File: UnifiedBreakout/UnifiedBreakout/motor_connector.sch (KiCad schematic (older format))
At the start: 1 part, among them J15 RJ45

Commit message: Unified breakout schematic "done"
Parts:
- J7: renamed from J15; footprint (none) -> Connector_RJ:RJ45_Ninigi_GE
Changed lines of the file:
@@
 $Descr A4 11693 8268
 encoding utf-8
-Sheet 2 5
+Sheet 3 20
 Title ""
 Date ""
@@
 $EndDescr
 $Comp
-L Connector:RJ45 J15
+L Connector:RJ45 J7
 U 1 1 5E675BA7
 P 5400 3350
-AR Path="/5E6754F3/5E675BA7" Ref="J15"  Part="1"
+AR Path="/5E6754F3/5E675BA7" Ref="J7"  Part="1"
 AR Path="/5E67ECBC/5E675BA7" Ref="J?"  Part="1"
-AR Path="/5E67FD54/5E675BA7" Ref="J?"  Part="1"
-AR Path="/5E67FFE4/5E675BA7" Ref="J?"  Part="1"
-F 0 "J?" H 5070 3354 50  0000 R CNN
+AR Path="/5E67FD54/5E675BA7" Ref="J8"  Part="1"
+AR Path="/5E67FFE4/5E675BA7" Ref="J9"  Part="1"
+F 0 "J9" H 5070 3354 50  0000 R CNN
 F 1 "RJ45" H 5070 3445 50  0000 R CNN
-F 2 "" V 5400 3375 50  0001 C CNN
+F 2 "Connector_RJ:RJ45_Ninigi_GE" V 5400 3375 50  0001 C CNN
 F 3 "~" V 5400 3375 50  0001 C CNN
 	1    5400 3350
@@
 Text HLabel 3500 3450 0    50   Input ~ 0
 ENABLE
-Text HLabel 3500 3650 0    50   Output ~ 0
+Text HLabel 3500 3650 0    50   Input ~ 0
 ALARM
 Text HLabel 4800 4000 3    50   UnSpc ~ 0

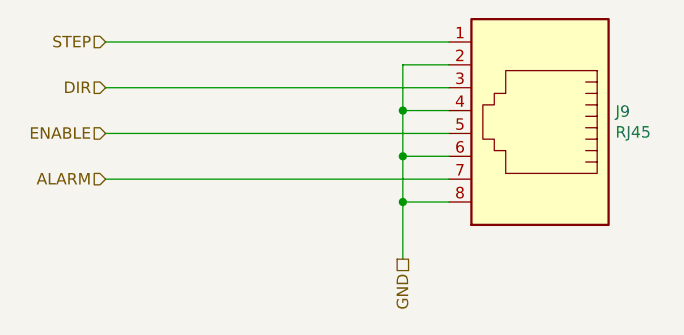
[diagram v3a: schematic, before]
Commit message: More placement, add some custom parts
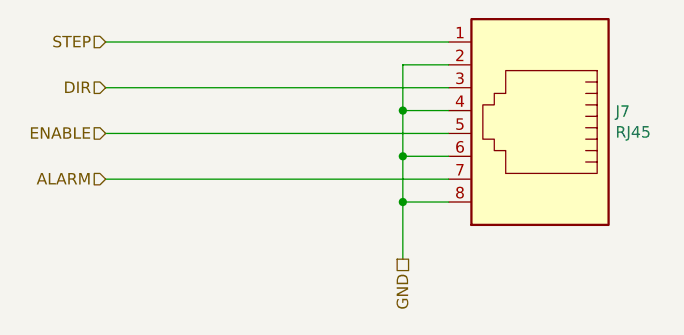
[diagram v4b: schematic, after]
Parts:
- J7: footprint Connector_RJ:RJ45_Ninigi_GE -> Stewart:SS6488SANF1
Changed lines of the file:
@@
 $Descr A4 11693 8268
 encoding utf-8
-Sheet 4 18
+Sheet 2 18
 Title ""
 Date ""
@@
 AR Path="/5E67FD54/5E675BA7" Ref="J8"  Part="1"
 AR Path="/5E67FFE4/5E675BA7" Ref="J9"  Part="1"
-F 0 "J9" H 5070 3354 50  0000 R CNN
+F 0 "J7" H 5070 3354 50  0000 R CNN
 F 1 "RJ45" H 5070 3445 50  0000 R CNN
-F 2 "Connector_RJ:RJ45_Ninigi_GE" V 5400 3375 50  0001 C CNN
+F 2 "Stewart:SS6488SANF1" V 5400 3375 50  0001 C CNN
 F 3 "~" V 5400 3375 50  0001 C CNN
 	1    5400 3350

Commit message: Assigned some parts
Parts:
- J7: MPN (none) -> SS-6488S-A-NF-1; Manufacturer (none) -> Bel
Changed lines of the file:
@@
 F 2 "Stewart:SS6488SANF1" V 5400 3375 50  0001 C CNN
 F 3 "~" V 5400 3375 50  0001 C CNN
+F 4 "SS-6488S-A-NF-1" H 5400 3350 50  0001 C CNN "MPN"
+F 5 "Bel" H 5400 3350 50  0001 C CNN "Manufacturer"
 	1    5400 3350
 	-1   0    0    1

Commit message: Finished(?) unified breakout layout
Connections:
- net ALARM: now also J7.8; no longer J7.7
- net DIR: now also J7.4; no longer J7.3
- net ENABLE: now also J7.6; no longer J7.5
- net GND: now also J7.1, J7.3, J7.5, J7.7; no longer J7.2, J7.4, J7.6, J7.8
- net STEP: now also J7.2; no longer J7.1
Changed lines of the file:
@@
 $EndComp
 Wire Wire Line
-	5000 3150 4800 3150
+	5000 3150 3500 3150
 Wire Wire Line
-	4800 3150 4800 3350
+	5000 3350 3500 3350
 Wire Wire Line
-	5000 3350 4800 3350
-Connection ~ 4800 3350
-Wire Wire Line
-	4800 3350 4800 3550
-Wire Wire Line
-	5000 3550 4800 3550
-Connection ~ 4800 3550
-Wire Wire Line
-	4800 3550 4800 3750
-Wire Wire Line
-	5000 3750 4800 3750
-Connection ~ 4800 3750
-Wire Wire Line
-	5000 3050 3500 3050
-Wire Wire Line
-	5000 3250 3500 3250
-Wire Wire Line
-	5000 3450 3500 3450
-Wire Wire Line
-	5000 3650 3500 3650
-Wire Wire Line
-	4800 3750 4800 4000
-Text HLabel 3500 3050 0    50   Input ~ 0
+	5000 3750 3500 3750
+Text HLabel 3500 3150 0    50   Input ~ 0
 STEP
-Text HLabel 3500 3250 0    50   Input ~ 0
+Text HLabel 3500 3350 0    50   Input ~ 0
 DIR
-Text HLabel 3500 3450 0    50   Input ~ 0
+Text HLabel 3500 3550 0    50   Input ~ 0
 ENABLE
-Text HLabel 3500 3650 0    50   Input ~ 0
+Text HLabel 3500 3750 0    50   Input ~ 0
 ALARM
 Text HLabel 4800 4000 3    50   UnSpc ~ 0
 GND
+Wire Wire Line
+	5000 3550 3500 3550
+Wire Wire Line
+	5000 3050 4800 3050
+Wire Wire Line
+	4800 3050 4800 3250
+Wire Wire Line
+	5000 3250 4800 3250
+Connection ~ 4800 3250
+Wire Wire Line
+	4800 3250 4800 3450
+Wire Wire Line
+	5000 3450 4800 3450
+Connection ~ 4800 3450
+Wire Wire Line
+	4800 3450 4800 3650
+Wire Wire Line
+	5000 3650 4800 3650
+Connection ~ 4800 3650
+Wire Wire Line
+	4800 3650 4800 4000
 $EndSCHEMATC

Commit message: Updated BOM
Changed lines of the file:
@@
 AR Path="/5E67FD54/5E675BA7" Ref="J8"  Part="1"
 AR Path="/5E67FFE4/5E675BA7" Ref="J9"  Part="1"
-F 0 "J7" H 5070 3354 50  0000 R CNN
+F 0 "J9" H 5070 3354 50  0000 R CNN
 F 1 "RJ45" H 5070 3445 50  0000 R CNN
 F 2 "Stewart:SS6488SANF1" V 5400 3375 50  0001 C CNN

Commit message: Final updates to unified BoB
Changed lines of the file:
@@
 AR Path="/5E67FD54/5E675BA7" Ref="J8"  Part="1"
 AR Path="/5E67FFE4/5E675BA7" Ref="J9"  Part="1"
-F 0 "J9" H 5070 3354 50  0000 R CNN
+F 0 "J7" H 5070 3354 50  0000 R CNN
 F 1 "RJ45" H 5070 3445 50  0000 R CNN
 F 2 "Stewart:SS6488SANF1" V 5400 3375 50  0001 C CNN
